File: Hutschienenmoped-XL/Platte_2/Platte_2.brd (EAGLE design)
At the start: 107.1 x 52.5 mm, 0 parts

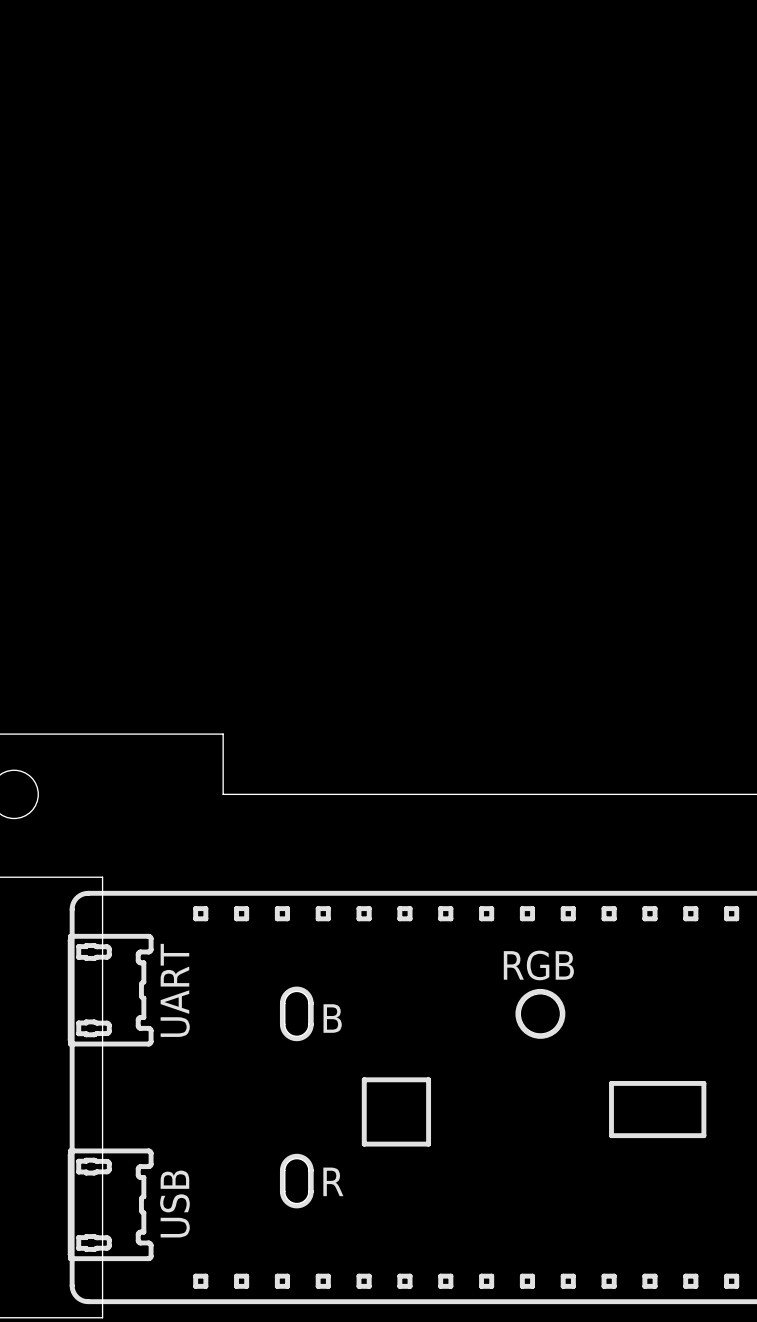
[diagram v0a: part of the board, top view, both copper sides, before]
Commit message: Adjust layer visibility and fill settings for multiple layers.
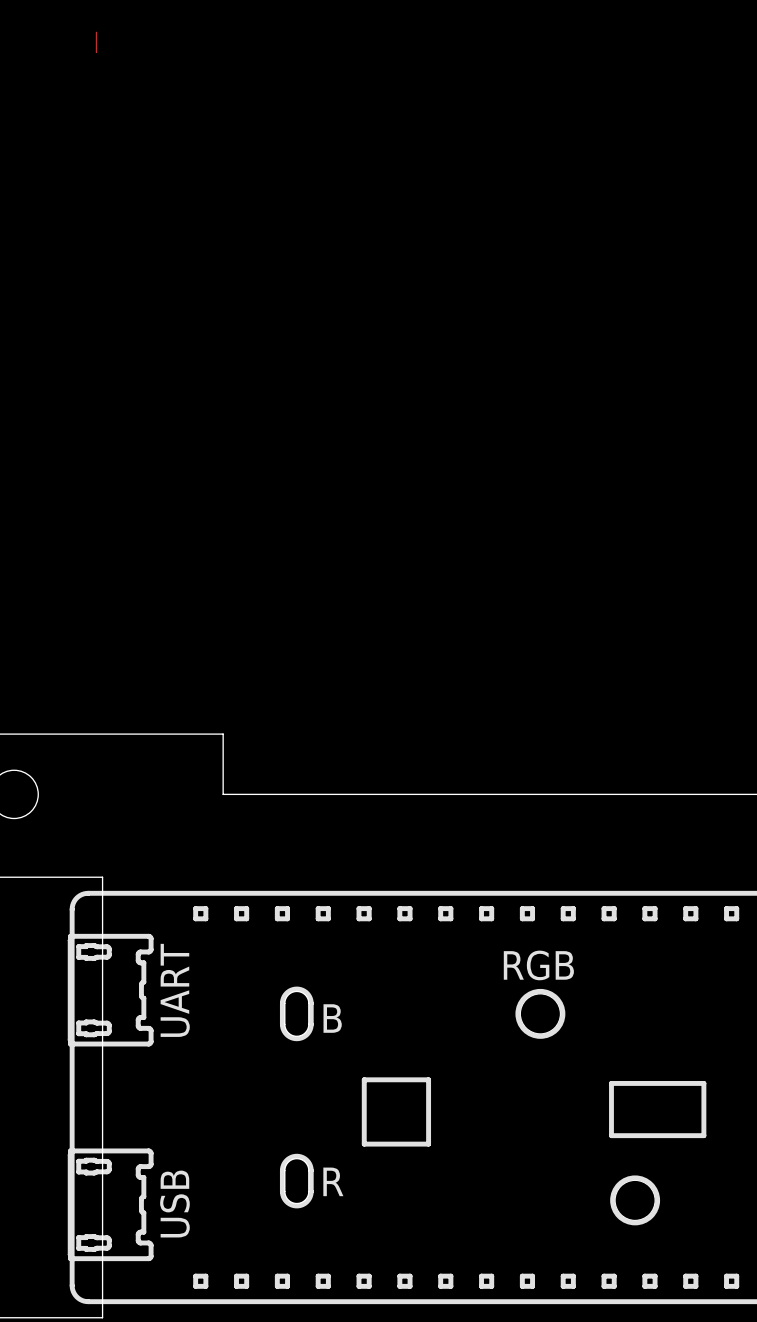
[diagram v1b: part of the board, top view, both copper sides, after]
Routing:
- net N$1: track 0.00 -> 1.27 mm
